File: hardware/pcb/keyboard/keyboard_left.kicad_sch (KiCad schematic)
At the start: 27 parts, among them J1 SM04B-SRSS-TB, J2 PJ320D, J3 HRO_TYPE-C-31-M-12, J4 FH34SRJ-10S-0.5SH, SW29 PTS845, U3 DT1446-04S, U4 XC6220B331MR-G, U5 STM32G0B1KETx, Y1 NX3215SA

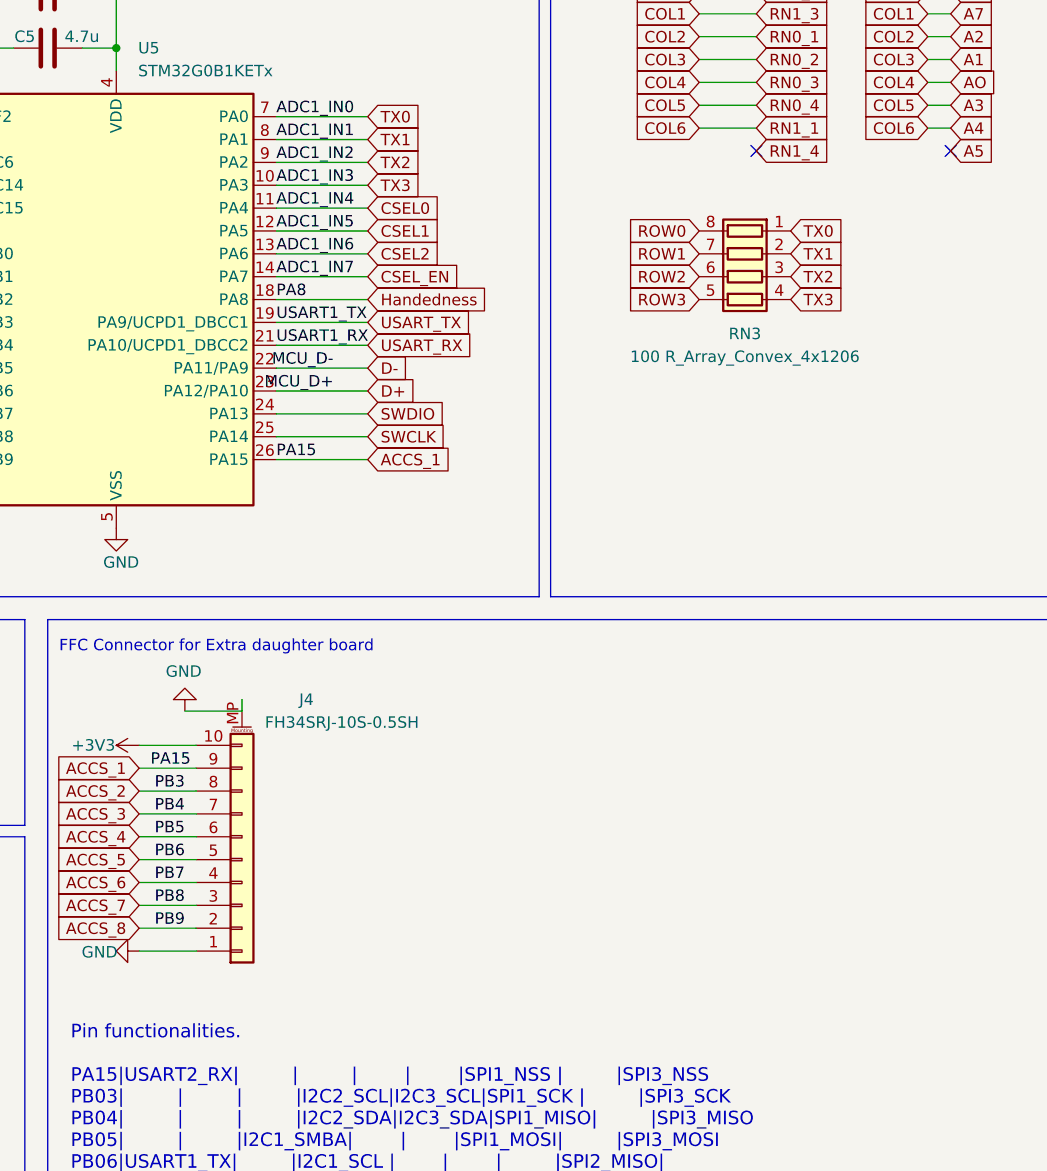
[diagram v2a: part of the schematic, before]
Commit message: roate FFC Connector
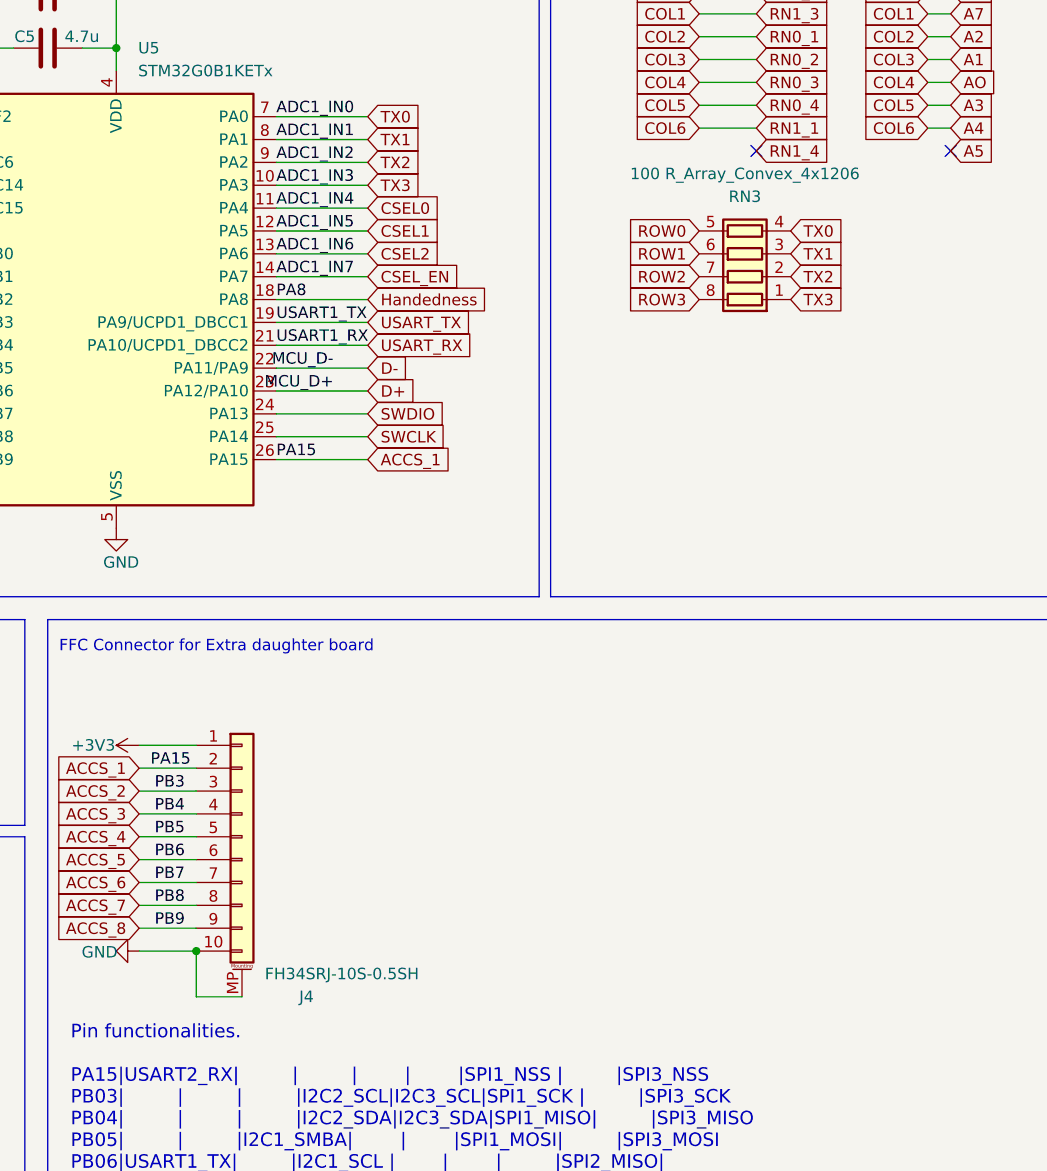
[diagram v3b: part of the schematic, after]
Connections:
- net +3V3: now also J4.1 (Pin_1); no longer J4.10 (Pin_10)
- net ACCS_1: now also J4.2 (Pin_2); no longer J4.9 (Pin_9)
- net ACCS_2: now also J4.3 (Pin_3); no longer J4.8 (Pin_8)
- net ACCS_3: now also J4.4 (Pin_4); no longer J4.7 (Pin_7)
- net ACCS_4: now also J4.5 (Pin_5); no longer J4.6 (Pin_6)
- net ACCS_5: now also J4.6 (Pin_6); no longer J4.5 (Pin_5)
- net ACCS_6: now also J4.7 (Pin_7); no longer J4.4 (Pin_4)
- net ACCS_7: now also J4.8 (Pin_8); no longer J4.3 (Pin_3)
- net ACCS_8: now also J4.9 (Pin_9); no longer J4.2 (Pin_2)
- net GND: now also J4.10 (Pin_10); no longer J4.1 (Pin_1)
- net ROW0: now also RN3.5 (R4.2); no longer RN3.8 (R1.2)
- net ROW1: now also RN3.6 (R3.2); no longer RN3.7 (R2.2)
- net ROW2: now also RN3.7 (R2.2); no longer RN3.6 (R3.2)
- net ROW3: now also RN3.8 (R1.2); no longer RN3.5 (R4.2)
- net TX0: now also RN3.4 (R4.1); no longer RN3.1 (R1.1)
- net TX1: now also RN3.3 (R3.1); no longer RN3.2 (R2.1)
- net TX2: now also RN3.2 (R2.1); no longer RN3.3 (R3.1)
- net TX3: now also RN3.1 (R1.1); no longer RN3.4 (R4.1)

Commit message: temp
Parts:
- removed R9 (x2): 1k, PCM_Resistor_SMD_AKL:R_0603_1608Metric_Pad0.98x0.95mm, symbol Device:R
- removed R9: < 800, PCM_Resistor_SMD_AKL:R_0603_1608Metric_Pad0.98x0.95mm, symbol Device:R
- removed U5: STM32G0B1KETx, PCM_Package_QFP_AKL:LQFP-32_7x7mm_P0.8mm, symbol MCU_ST_STM32G0:STM32G0B1KETx
- removed Y1: NX3215SA, PCM_Crystal_AKL:Crystal_SMD_3215-2Pin_3.2x1.5mm, symbol Device:Crystal
- added C11: 1uF, PCM_Capacitor_SMD_AKL:C_0603_1608Metric, symbol Device:C
- added C12, C13: 22p, PCM_Capacitor_SMD_AKL:C_0603_1608Metric, symbol Device:C
- added C16: 100n, PCM_Capacitor_SMD_AKL:C_0603_1608Metric, symbol Device:C
- added C17: 1u, PCM_Capacitor_SMD_AKL:C_0603_1608Metric, symbol Device:C
- added FB1: 1k 100mhz, Inductor_SMD:L_0603_1608Metric, symbol Device:FerriteBead
- added R9: 10k, PCM_Resistor_SMD_AKL:R_0603_1608Metric, symbol Device:R
- added U5: STM32G431KBTx, Package_QFP:LQFP-32_7x7mm_P0.8mm, symbol MCU_ST_STM32G4:STM32G431KBTx
- added U6: CH334R, Package_SO:QSOP-16_3.9x4.9mm_P0.635mm, symbol wch_mcu_peripheral:CH334R
- added Y1, Y2: 8MHz, PCM_Crystal_Handsoldering_AKL:Crystal_SMD_2520-4Pin_2.5x2.0mm, symbol Device:Crystal_GND24_Small
- C1, C20, C21, C4, C6, C7: footprint PCM_Capacitor_SMD_AKL:C_0603_1608Metric_Pad1.05x0.95mm -> PCM_Capacitor_SMD_AKL:C_0603_1608Metric
- C5: value 4.7u -> 0.1uF; footprint PCM_Capacitor_SMD_AKL:C_0603_1608Metric_Pad1.05x0.95mm -> PCM_Capacitor_SMD_AKL:C_0603_1608Metric
- R9: footprint PCM_Resistor_SMD_AKL:R_0603_1608Metric_Pad0.98x0.95mm -> PCM_Resistor_SMD_AKL:R_0603_1608Metric
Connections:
- net ACCS_8 is gone; now on net ACCS_7: J4.9 (Pin_9)
- net +3V3: now also J1.1 (Pin_1), TP1.1 (Pin_1), FB1.2, R9.2, U5.1 (VDD), U5.17 (VDD)
- net +5V: no longer J1.1 (Pin_1), TP1.1 (Pin_1)
- net ACCS_1: now also J4.3 (Pin_3), U5.25 (PA15); no longer J4.2 (Pin_2)
- net ACCS_2: now also J4.4 (Pin_4), U5.26 (PB3); no longer J4.3 (Pin_3)
- net ACCS_3: now also J4.5 (Pin_5), U5.27 (PB4); no longer J4.4 (Pin_4)
- net ACCS_4: now also J4.6 (Pin_6), U5.28 (PB5); no longer J4.5 (Pin_5)
- net ACCS_5: now also J4.7 (Pin_7), U5.29 (PB6); no longer J4.6 (Pin_6)
- net ACCS_6: now also J4.8 (Pin_8), U5.30 (PB7); no longer J4.7 (Pin_7)
- net ACCS_7: now also U5.31 (PB8); no longer J4.8 (Pin_8)
- net ADC: now also U5.13 (PB0)
- net CHARGE_RST: now also U5.18 (PA8)
- net CSEL0: now also U5.9 (PA4)
- net CSEL1: now also U5.10 (PA5)
- net CSEL2: now also U5.11 (PA6)
- net CSEL_EN: now also U5.12 (PA7)
- net GND: now also C11.2, C12.1, C13.1, C16.2, C17.2, U5.14 (VSSA), U5.16 (VSS), U5.32 (VSS), U6.14 (GND), Y1.2, Y1.4, Y2.2, Y2.4
- net NRST: now also R9.1, U5.4 (PG10)
- net SWCLK: now also U5.24 (PA14)
- net SWDIO: now also U5.23 (PA13)
- net TX0: now also U5.5 (PA0)
- net TX1: now also U5.6 (PA1)
- net TX2: now also U5.7 (PA2)
- net TX3: now also U5.8 (PA3)
- net USART_RX: now also U3.1 (IO1), U5.20 (PA10); no longer U3.4 (IO3)
- net USART_TX: now also U5.19 (PA9)
- net VBUS: now also D1.2 (A), F1.1, C11.1, U6.12 (V5); no longer F1.2, J3.A4 (VBUS), J3.A9 (VBUS), J3.B4 (VBUS), J3.B9 (VBUS)
- net VDDA: now also C16.1, C17.1, FB1.1, U5.15 (VDDA)
- net D+ renamed UP_D+
- net UP_D+: now also U6.11 (DPU)
- net D- renamed UP_D-
- net UP_D-: now also U3.4 (IO3), U6.10 (DMU); no longer U3.1 (IO1)
- net OSC32_IN: no longer names the net of C6.2
- net OSC32_IN: now also U5.2 (PF0), Y1.3
- net OSC32_OUT: no longer names the net of C7.2
- net OSC32_OUT: now also U5.3 (PF1), Y1.1
- new net: C12.2, U6.15 (XO), Y2.3
- new net: C13.2, U6.16 (XI), Y2.1
- new net: F1.2, J3.A4 (VBUS), J3.A9 (VBUS), J3.B4 (VBUS), J3.B9 (VBUS)
- new net MCU_D+: U5.22 (PA12), U6.8 (DP1)
- new net MCU_D-: U5.21 (PA11), U6.7 (DM1)
- no-connect marks 9 -> 10
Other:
- note removed: "(32.768kHz)"
- note removed: "To simplified route, Handedness pin connected with vbus pin. Use less than 800ohm resistor for R4, To both of pin's voltages is greater than 1.7v."
- moved on the sheet: C4, C5, C6, C7

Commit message: Left init
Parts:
- removed J4: FH34SRJ-10S-0.5SH, ec_parts:HRS_FH34SRJ-10S-0.5SH(50), symbol Connector_Generic_MountingPin:Conn_01x10_MountingPin
- added C14: 1uF, PCM_Capacitor_SMD_AKL:C_0603_1608Metric, symbol Device:C
- added C15: 4.7 uF, PCM_Capacitor_SMD_AKL:C_0603_1608Metric, symbol Device:C
- added J4: FH34SRJ-10S-0.5SH, ec_parts:HRS_FH34SRJ-12S-0.5SH(50), symbol Connector_Generic_MountingPin:Conn_01x12_MountingPin
- C16: value 100n -> 10n
- FB1: value 1k 100mhz -> 1kΩ 100mhz
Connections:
- net +3V3: now also C15.1, J4.4 (Pin_4)
- net ACCS_1: now also J4.5 (Pin_5)
- net ACCS_2: now also J4.6 (Pin_6)
- net ACCS_3: now also J4.7 (Pin_7)
- net ACCS_4: now also J4.8 (Pin_8)
- net ACCS_5: now also J4.9 (Pin_9)
- net ACCS_6: now also J4.10 (Pin_10)
- net ACCS_7: now also J4.11 (Pin_11)
- net GND: now also C14.2, C15.2, J4.12 (Pin_12), J4.MP (MountPin)
- net VBUS: now also J4.1 (Pin_1)
- net DM4: now reaches U6.1 (DM4)
- net DM4: now also J4.2 (Pin_2)
- net at U6.13 (VDD33): now also C14.1
- net DP4: now reaches U6.2 (DP4)
- net DP4: now also J4.3 (Pin_3)
- no-connect marks 10 -> 9
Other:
- moved on the sheet: C11, C12, C13, C20, C21, C4, C5, D1, F1, FB1, H17, J3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

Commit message: Right init
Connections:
- net ADC: now also U5.12 (PA7); no longer U5.13 (PB0)
- net CHARGE_RST: now also U5.13 (PB0); no longer U5.18 (PA8)
- net CSEL_EN: now also U5.18 (PA8); no longer U5.12 (PA7)
- no-connect marks 9 -> 8
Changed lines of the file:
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@@
   (junction (at 69.85 92.71) (diameter 0) (color 0 0 0 0)
   )
-  (no_connect (at 273.05 41.91))
   (no_connect (at 41.91 59.69))
   (no_connect (at 251.46 41.91))
@@
     (stroke (width 0) (type default))
   )
+  (wire (pts (xy 270.51 41.91) (xy 273.05 41.91))
+    (stroke (width 0) (type default))
+  )
   (wire (pts (xy 171.45 25.4) (xy 168.91 25.4))
     (stroke (width 0) (type default))
@@
     (effects (font (size 1.27 1.27)) (justify right bottom))
   )
+  (global_label "ADC" (shape input) (at 208.28 55.88 0) (fields_autoplaced)
+    (effects (font (size 1.27 1.27)) (justify left))
+    (property "Intersheetrefs" "${INTERSHEET_REFS}" (at 213.5971 55.88 0)
+      (effects (font (size 1.27 1.27)) (justify left) hide)
+    )
+  )
   (global_label "SWDIO" (shape input) (at 208.28 71.12 0) (fields_autoplaced)
     (effects (font (size 1.27 1.27)) (justify left))
@@
     )
   )
-  (global_label "CSEL_EN" (shape input) (at 208.28 55.88 0) (fields_autoplaced)
-    (effects (font (size 1.27 1.27)) (justify left))
-    (property "Intersheetrefs" "${INTERSHEET_REFS}" (at 217.8753 55.88 0)
+  (global_label "CSEL_EN" (shape input) (at 208.28 58.42 0) (fields_autoplaced)
+    (effects (font (size 1.27 1.27)) (justify left))
+    (property "Intersheetrefs" "${INTERSHEET_REFS}" (at 217.8753 58.42 0)
       (effects (font (size 1.27 1.27)) (justify left) hide)
     )
@@
     )
   )
-  (global_label "ADC" (shape input) (at 162.56 50.8 180) (fields_autoplaced)
-    (effects (font (size 1.27 1.27)) (justify right))
-    (property "Intersheetrefs" "${INTERSHEET_REFS}" (at 157.2429 50.8 0)
-      (effects (font (size 1.27 1.27)) (justify right) hide)
-    )
-  )
   (global_label "ACCS_3" (shape input) (at 182.88 118.11 180) (fields_autoplaced)
     (effects (font (size 1.27 1.27)) (justify right))
@@
     )
   )
+  (global_label "CHARGE_RST" (shape input) (at 162.56 50.8 180) (fields_autoplaced)
+    (effects (font (size 1.27 1.27)) (justify right))
+    (property "Intersheetrefs" "${INTERSHEET_REFS}" (at 149.7562 50.8 0)
+      (effects (font (size 1.27 1.27)) (justify right) hide)
+    )
+  )
   (global_label "TX2" (shape input) (at 255.27 55.88 0) (fields_autoplaced)
     (effects (font (size 1.27 1.27)) (justify left))
@@
     (property "Intersheetrefs" "${INTERSHEET_REFS}" (at 223.52 166.37 0)
       (effects (font (size 1.27 1.27)) hide)
-    )
-  )
-  (global_label "CHARGE_RST" (shape input) (at 208.28 58.42 0) (fields_autoplaced)
-    (effects (font (size 1.27 1.27)) (justify left))
-    (property "Intersheetrefs" "${INTERSHEET_REFS}" (at 221.0838 58.42 0)
-      (effects (font (size 1.27 1.27)) (justify left) hide)
     )
   )
@@
         )
       )
+    )
+  )
+  (symbol (lib_id "power:GNDA") (at 270.51 41.91 270) (unit 1)
+    (in_bom yes) (on_board yes) (dnp no)
+    (property "Reference" "#PWR052" (at 264.16 41.91 0)
+      (effects (font (size 1.27 1.27)) hide)
+    )
+    (property "Value" "GNDA" (at 266.7 41.91 90)
+      (effects (font (size 1.27 1.27)) (justify right))
+    )
+    (property "Footprint" "" (at 270.51 41.91 0)
+      (effects (font (size 1.27 1.27)) hide)
+    )
+    (property "Datasheet" "" (at 270.51 41.91 0)
+      (effects (font (size 1.27 1.27)) hide)
+    )
+    (pin "1")
+    (instances
+      (project "keyboard_left"
+        (path "/852dabbf-de45-4470-8176-59d37a754407"
+          (reference "#PWR052") (unit 1)
+        )
+        (path "/852dabbf-de45-4470-8176-59d37a754407/ac97752b-a16f-44ee-ad7e-0bcdbcea7979"
+          (reference "#PWR043") (unit 1)
+        )
+      )

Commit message: usb hib init
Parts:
- added R9: 10k, PCM_Resistor_SMD_AKL:R_0603_1608Metric, symbol Device:R
- added R9: 5.1k, PCM_Resistor_SMD_AKL:R_0603_1608Metric, symbol Device:R
- J4: value FH34SRJ-10S-0.5SH -> FH34SRJ-12S-0.5SH
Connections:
- net ACCS_3: now also R9.1, R9.2
- net GND: now also R9.1
- net VBUS: now also R9.2
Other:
- note added: "ACCS_3(SPI MISO) can be used as a extra GPIO or VBUS/USB connection detect"
- note added: "Pin functionalities. PA15 |I2C1_SCL |SPI1_NSS |SPI3_NSS | |USART2_RX PB3 | |SPI1_SCK |SPI3_SCK | |USART2_TX PB4 | |SPI1_MISO|SPI3_MISO| |USART2_RX PB5 | |SPI1_MOSI|SPI3_MOSI| |USART2_CK PB6 | | | |USART1_TX| PB7 |I2C1_SDA | | |USART1_RX| PB8-BOOT0|I2C1_SCL | | |"
- note removed: "Pin functionalities. PA15|USART2_RX| | | | |SPI1_NSS | |SPI3_NSS PB03| | | |I2C2_SCL|I2C3_SCL|SPI1_SCK | |SPI3_SCK PB04| | | |I2C2_SDA|I2C3_SDA|SPI1_MISO| |SPI3_MISO PB05| | |I2C1_SMBA| | |SPI1_MOSI| |SPI3_MOSI PB06|USART1_TX| |I2C1_SCL | | | |SPI2_MISO| PB07|USART1_RX| |I2C1_SDA | | | |SPI2_MOSI| PB08| |USART3_TX|I2C1_SCL | | | |SPI2_SCK | PB09| |USART3_RX|I2C1_SDA | | | |SPI2_NSS |"
- moved on the sheet: J4
